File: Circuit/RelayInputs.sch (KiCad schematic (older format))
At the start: 6 parts, among them K301 Meisei-m4-24h, K302 Meisei-m4-24h, K303 Meisei-m4-24h, K304 Meisei-m4-24h, K305 Meisei-m4-24h, K306 Meisei-m4-24h

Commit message: Continued PCB work, placement started. Report and presentation also started
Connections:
- net GND: no longer K301.4 (T1common), K302.4 (T1common), K303.4 (T1common), K304.4 (T1common), K305.4 (T1common), K306.4 (T1common)
- net Input1: now also K301.4 (T1common); no longer K301.8 (T1sel2)
- net Input2: now also K302.4 (T1common); no longer K302.8 (T1sel2)
- net Input3: now also K303.4 (T1common); no longer K303.8 (T1sel2)
- net Input4: now also K304.4 (T1common); no longer K304.8 (T1sel2)
- net Input5: now also K305.4 (T1common); no longer K305.8 (T1sel2)
- net Input6: now also K306.4 (T1common); no longer K306.8 (T1sel2)
- new net +3V3: K301.8 (T1sel2), K302.8 (T1sel2), K303.8 (T1sel2), K304.8 (T1sel2), K305.8 (T1sel2), K306.8 (T1sel2)
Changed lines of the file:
@@
 EESchema Schematic File Version 2
+LIBS:ControlCircuit-rescue
 LIBS:power
 LIBS:device
@@
 L GND #PWR031
 U 1 1 58AE5323
-P 2950 2450
-F 0 "#PWR031" H 2950 2200 50  0001 C CNN
-F 1 "GND" H 2950 2300 50  0000 C CNN
-F 2 "" H 2950 2450 50  0000 C CNN
-F 3 "" H 2950 2450 50  0000 C CNN
-	1    2950 2450
-	0    1    1    0
-$EndComp
-Wire Wire Line
-	2900 2650 3100 2650
+P 2850 2550
+F 0 "#PWR031" H 2850 2300 50  0001 C CNN
+F 1 "GND" H 2850 2400 50  0000 C CNN
+F 2 "" H 2850 2550 50  0000 C CNN
+F 3 "" H 2850 2550 50  0000 C CNN
+	1    2850 2550
+	0    1    1    0
+$EndComp
 Wire Wire Line
 	3050 2250 3050 2300
 Wire Wire Line
 	3050 2300 3100 2300
-Wire Wire Line
-	2950 2450 3100 2450
-Wire Wire Line
-	3100 2550 3050 2550
-Wire Wire Line
-	3050 2550 3050 2450
-Connection ~ 3050 2450
-Text GLabel 2900 2650 0    60   Input ~ 0
+Text GLabel 2800 2300 0    60   Input ~ 0
 Input1
 NoConn ~ 4400 2450
@@
 L GND #PWR033
 U 1 1 58AE5388
-P 2950 3650
-F 0 "#PWR033" H 2950 3400 50  0001 C CNN
-F 1 "GND" H 2950 3500 50  0000 C CNN
-F 2 "" H 2950 3650 50  0000 C CNN
-F 3 "" H 2950 3650 50  0000 C CNN
-	1    2950 3650
-	0    1    1    0
-$EndComp
-Wire Wire Line
-	2900 3850 3100 3850
+P 2850 3750
+F 0 "#PWR033" H 2850 3500 50  0001 C CNN
+F 1 "GND" H 2850 3600 50  0000 C CNN
+F 2 "" H 2850 3750 50  0000 C CNN
+F 3 "" H 2850 3750 50  0000 C CNN
+	1    2850 3750
+	0    1    1    0
+$EndComp
 Wire Wire Line
 	3050 3450 3050 3500
 Wire Wire Line
 	3050 3500 3100 3500
-Wire Wire Line
-	2950 3650 3100 3650
-Wire Wire Line
-	3100 3750 3050 3750
-Wire Wire Line
-	3050 3750 3050 3650
-Connection ~ 3050 3650
-Text GLabel 2900 3850 0    60   Input ~ 0
+Text GLabel 2800 3500 0    60   Input ~ 0
 Input2
 NoConn ~ 4400 3650
@@
 L GND #PWR035
 U 1 1 58AE53E8
-P 2950 4800
-F 0 "#PWR035" H 2950 4550 50  0001 C CNN
-F 1 "GND" H 2950 4650 50  0000 C CNN
-F 2 "" H 2950 4800 50  0000 C CNN
-F 3 "" H 2950 4800 50  0000 C CNN
-	1    2950 4800
-	0    1    1    0
-$EndComp
-Wire Wire Line
-	2900 5000 3100 5000
+P 2850 4900
+F 0 "#PWR035" H 2850 4650 50  0001 C CNN
+F 1 "GND" H 2850 4750 50  0000 C CNN
+F 2 "" H 2850 4900 50  0000 C CNN
+F 3 "" H 2850 4900 50  0000 C CNN
+	1    2850 4900
+	0    1    1    0
+$EndComp
 Wire Wire Line
 	3050 4600 3050 4650
 Wire Wire Line
 	3050 4650 3100 4650
-Wire Wire Line
-	2950 4800 3100 4800
-Wire Wire Line
-	3100 4900 3050 4900
-Wire Wire Line
-	3050 4900 3050 4800
-Connection ~ 3050 4800
-Text GLabel 2900 5000 0    60   Input ~ 0
+Text GLabel 2800 4650 0    60   Input ~ 0
 Input3
 NoConn ~ 4400 4800
@@
 L GND #PWR037
 U 1 1 58AE54DC
-P 6200 2450
-F 0 "#PWR037" H 6200 2200 50  0001 C CNN
-F 1 "GND" H 6200 2300 50  0000 C CNN
-F 2 "" H 6200 2450 50  0000 C CNN
-F 3 "" H 6200 2450 50  0000 C CNN
-	1    6200 2450
-	0    1    1    0
-$EndComp
-Wire Wire Line
-	6150 2650 6350 2650
+P 6100 2550
+F 0 "#PWR037" H 6100 2300 50  0001 C CNN
+F 1 "GND" H 6100 2400 50  0000 C CNN
+F 2 "" H 6100 2550 50  0000 C CNN
+F 3 "" H 6100 2550 50  0000 C CNN
+	1    6100 2550
+	0    1    1    0
+$EndComp
 Wire Wire Line
 	6300 2250 6300 2300
 Wire Wire Line
 	6300 2300 6350 2300
-Wire Wire Line
-	6200 2450 6350 2450
-Wire Wire Line
-	6350 2550 6300 2550
-Wire Wire Line
-	6300 2550 6300 2450
-Connection ~ 6300 2450
-Text GLabel 6150 2650 0    60   Input ~ 0
+Text GLabel 6050 2300 0    60   Input ~ 0
 Input4
 NoConn ~ 7650 2450
@@
 L GND #PWR039
 U 1 1 58AE54FB
-P 6200 3650
-F 0 "#PWR039" H 6200 3400 50  0001 C CNN
-F 1 "GND" H 6200 3500 50  0000 C CNN
-F 2 "" H 6200 3650 50  0000 C CNN
-F 3 "" H 6200 3650 50  0000 C CNN
-	1    6200 3650
-	0    1    1    0
-$EndComp
-Wire Wire Line
-	6150 3850 6350 3850
+P 6100 3750
+F 0 "#PWR039" H 6100 3500 50  0001 C CNN
+F 1 "GND" H 6100 3600 50  0000 C CNN
+F 2 "" H 6100 3750 50  0000 C CNN
+F 3 "" H 6100 3750 50  0000 C CNN
+	1    6100 3750
+	0    1    1    0
+$EndComp
 Wire Wire Line
 	6300 3450 6300 3500
 Wire Wire Line
 	6300 3500 6350 3500
-Wire Wire Line
-	6200 3650 6350 3650
-Wire Wire Line
-	6350 3750 6300 3750
-Wire Wire Line
-	6300 3750 6300 3650
-Connection ~ 6300 3650
-Text GLabel 6150 3850 0    60   Input ~ 0
+Text GLabel 6050 3500 0    60   Input ~ 0
 Input5
 NoConn ~ 7650 3650
@@
 L GND #PWR041
 U 1 1 58AE551A
-P 6200 4800
-F 0 "#PWR041" H 6200 4550 50  0001 C CNN
-F 1 "GND" H 6200 4650 50  0000 C CNN
-F 2 "" H 6200 4800 50  0000 C CNN
-F 3 "" H 6200 4800 50  0000 C CNN
-	1    6200 4800
-	0    1    1    0
-$EndComp
-Wire Wire Line
-	6150 5000 6350 5000
+P 6150 4900
+F 0 "#PWR041" H 6150 4650 50  0001 C CNN
+F 1 "GND" H 6150 4750 50  0000 C CNN
+F 2 "" H 6150 4900 50  0000 C CNN
+F 3 "" H 6150 4900 50  0000 C CNN
+	1    6150 4900
+	0    1    1    0
+$EndComp
 Wire Wire Line
 	6300 4600 6300 4650
 Wire Wire Line
 	6300 4650 6350 4650
-Wire Wire Line
-	6200 4800 6350 4800
-Wire Wire Line
-	6350 4900 6300 4900
-Wire Wire Line
-	6300 4900 6300 4800
-Connection ~ 6300 4800
-Text GLabel 6150 5000 0    60   Input ~ 0
+Text GLabel 6050 4650 0    60   Input ~ 0
 Input6
 NoConn ~ 7650 4800
@@
 Text Notes 2450 5500 0    60   ~ 0
 Relay Inputs
+$Comp
+L +3.3V #PWR?
+U 1 1 58AEEFB8
+P 6150 5150
+F 0 "#PWR?" H 6150 5000 50  0001 C CNN
+F 1 "+3.3V" H 6150 5290 50  0000 C CNN
+F 2 "" H 6150 5150 50  0000 C CNN
+F 3 "" H 6150 5150 50  0000 C CNN
+	1    6150 5150
+	0    -1   -1   0
+$EndComp
+Wire Wire Line
+	6050 4650 6200 4650
+Wire Wire Line
+	6150 4900 6350 4900
+Wire Wire Line
+	6200 4650 6200 4800
+Wire Wire Line
+	6200 4800 6350 4800
+Wire Wire Line
+	6150 5150 6200 5150
+Wire Wire Line
+	6200 5150 6200 5000
+Wire Wire Line
+	6200 5000 6350 5000
+$Comp
+L +3.3V #PWR?
+U 1 1 58AEF2C8
+P 6100 4000
+F 0 "#PWR?" H 6100 3850 50  0001 C CNN
+F 1 "+3.3V" H 6100 4140 50  0000 C CNN
+F 2 "" H 6100 4000 50  0000 C CNN
+F 3 "" H 6100 4000 50  0000 C CNN
+	1    6100 4000
+	0    -1   -1   0
+$EndComp
+$Comp
+L +3.3V #PWR?
+U 1 1 58AEF2E5
+P 6100 2800
+F 0 "#PWR?" H 6100 2650 50  0001 C CNN
+F 1 "+3.3V" H 6100 2940 50  0000 C CNN
+F 2 "" H 6100 2800 50  0000 C CNN
+F 3 "" H 6100 2800 50  0000 C CNN
+	1    6100 2800
+	0    -1   -1   0
+$EndComp
+$Comp
+L +3.3V #PWR?
+U 1 1 58AEF31A
+P 2850 2800
+F 0 "#PWR?" H 2850 2650 50  0001 C CNN
+F 1 "+3.3V" H 2850 2940 50  0000 C CNN
+F 2 "" H 2850 2800 50  0000 C CNN
+F 3 "" H 2850 2800 50  0000 C CNN
+	1    2850 2800
+	0    -1   -1   0
+$EndComp
+$Comp
+L +3.3V #PWR?
+U 1 1 58AEF337
+P 2850 4000
+F 0 "#PWR?" H 2850 3850 50  0001 C CNN
+F 1 "+3.3V" H 2850 4140 50  0000 C CNN
+F 2 "" H 2850 4000 50  0000 C CNN
+F 3 "" H 2850 4000 50  0000 C CNN
+	1    2850 4000
+	0    -1   -1   0
+$EndComp
+$Comp
+L +3.3V #PWR?
+U 1 1 58AEF370
+P 2850 5150
+F 0 "#PWR?" H 2850 5000 50  0001 C CNN
+F 1 "+3.3V" H 2850 5290 50  0000 C CNN
+F 2 "" H 2850 5150 50  0000 C CNN
+F 3 "" H 2850 5150 50  0000 C CNN
+	1    2850 5150
+	0    -1   -1   0
+$EndComp
+Wire Wire Line
+	6100 3750 6350 3750
+Wire Wire Line
+	6050 3500 6150 3500
+Wire Wire Line
+	6150 3500 6150 3650
+Wire Wire Line
+	6150 3650 6350 3650
+Wire Wire Line
+	6100 4000 6150 4000
+Wire Wire Line
+	6150 4000 6150 3850
+Wire Wire Line
+	6150 3850 6350 3850
+Wire Wire Line
+	6050 2300 6150 2300
+Wire Wire Line
+	6150 2300 6150 2450
+Wire Wire Line
+	6150 2450 6350 2450
+Wire Wire Line
+	6100 2550 6350 2550
+Wire Wire Line
+	6100 2800 6150 2800
+Wire Wire Line
+	6150 2800 6150 2650
+Wire Wire Line
+	6150 2650 6350 2650
+Wire Wire Line
+	2800 2300 2900 2300
+Wire Wire Line
+	2900 2300 2900 2450
+Wire Wire Line
+	2900 2450 3100 2450
+Wire Wire Line
+	2850 2550 3100 2550
+Wire Wire Line
+	2850 2800 2900 2800
+Wire Wire Line
+	2900 2800 2900 2650
+Wire Wire Line
+	2900 2650 3100 2650
+Wire Wire Line
+	2800 3500 2900 3500
+Wire Wire Line
+	2900 3500 2900 3650
+Wire Wire Line
+	2900 3650 3100 3650
+Wire Wire Line
+	2850 3750 3100 3750
+Wire Wire Line
+	2850 4000 2900 4000
+Wire Wire Line
+	2900 4000 2900 3850
+Wire Wire Line
+	2900 3850 3100 3850
+Wire Wire Line
+	2800 4650 2900 4650
+Wire Wire Line
+	2900 4650 2900 4800
+Wire Wire Line
+	2900 4800 3100 4800
+Wire Wire Line
+	2850 4900 3100 4900
+Wire Wire Line
+	2850 5150 2900 5150
+Wire Wire Line
+	2900 5150 2900 5000
+Wire Wire Line
+	2900 5000 3100 5000
 $EndSCHEMATC

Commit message: Additional PCB work
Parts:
- added D? (x2): D, symbol D
- added K307, K308: Meisei-m4-24h, Meisei:Meisei-m4-24h, symbol Meisei-m4-24h
- added R? (x2): 2kR, symbol R
- added U301, U?: LTV-817, DIP-4, symbol LTV-817
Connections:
- net +3V3: now also K307.8 (T1sel2), K308.8 (T1sel2)
- net GND: now also K307.6 (T1sel1), K308.6 (T1sel1), U301.3, U?.3
- net GNDREF: now also K307.1 (Coil1), K308.1 (Coil1)
- net Input1 renamed I1
- net Input2 renamed I2
- net Input3 renamed I3
- net Input4 renamed I4
- net Input5 renamed I5
- net I5: now also U301.4
- net Input6 renamed I6
- net I6: now also U?.4
- net RelayInput1 renamed RI1
- net RelayInput2 renamed RI2
- net RelayInput3 renamed RI3
- net RelayInput4 renamed RI4
- net RelayInput5 renamed RI5
- net RelayInput6 renamed RI6
- new net: D?.1 (K), R?.1, U301.1
- new net: D?.1 (K), R?.1, U?.1
- new net I7: K307.4 (T1common)
- new net I8: K308.4 (T1common)
- new net RI5A: R?.2
- new net RI5K: D?.2 (A), U301.2
- new net RI6A: R?.2
- new net RI6K: D?.2 (A), U?.2
- new net RI7: K307.16 (Coil2)
- new net RI8: K308.16 (Coil2)
- no-connect marks 18 -> 24
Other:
- moved on the sheet: K301, K302, K303, K304, K305, K306

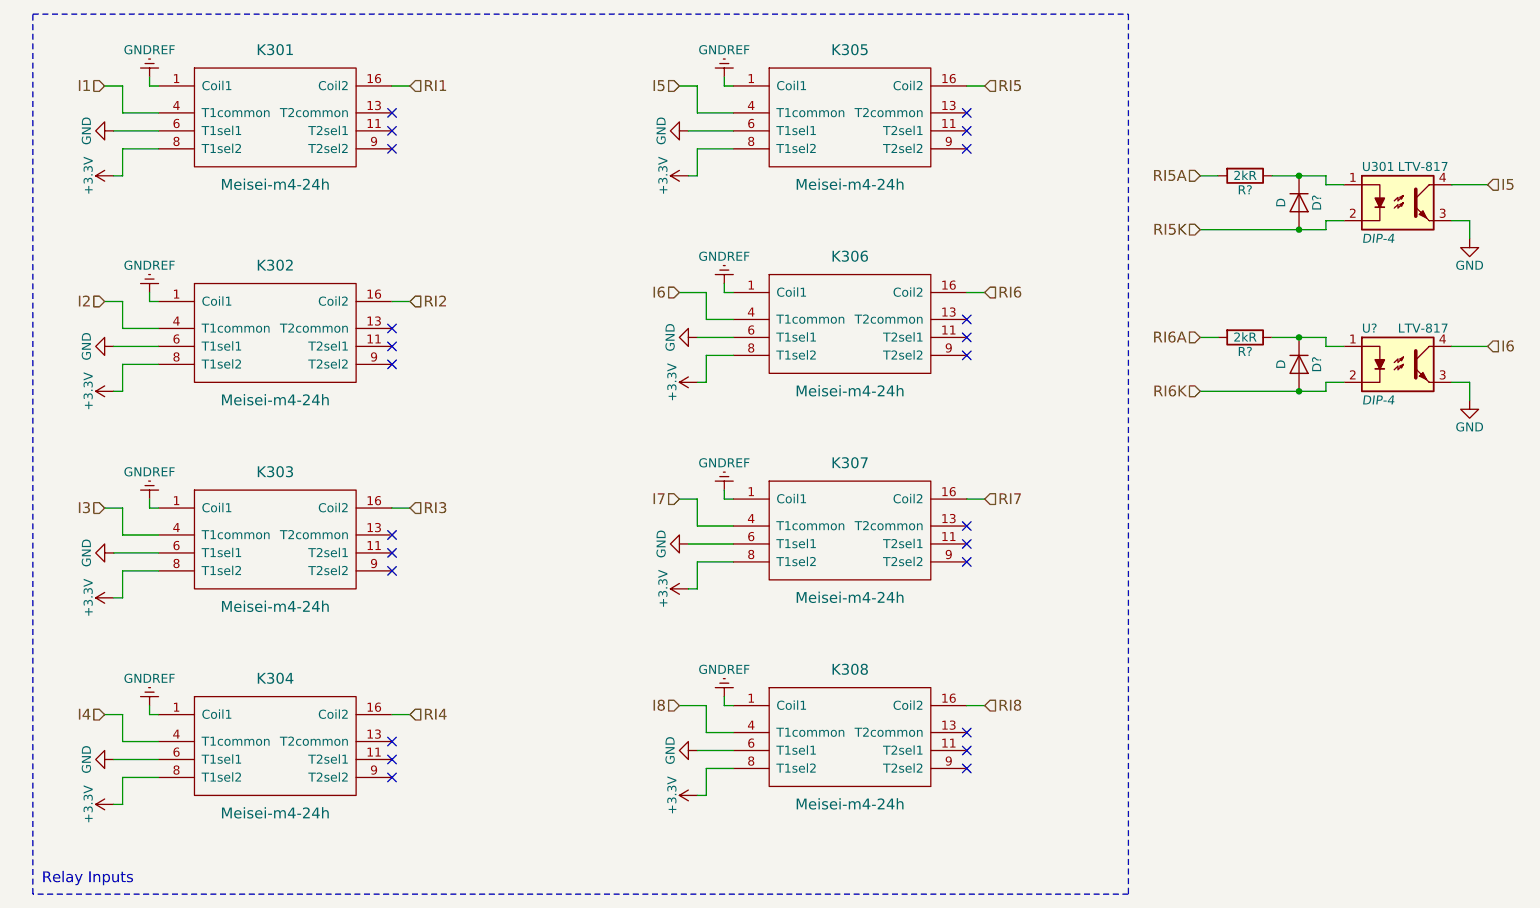
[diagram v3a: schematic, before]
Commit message: Routed PCB and made backup. Footprint for Optocouplers
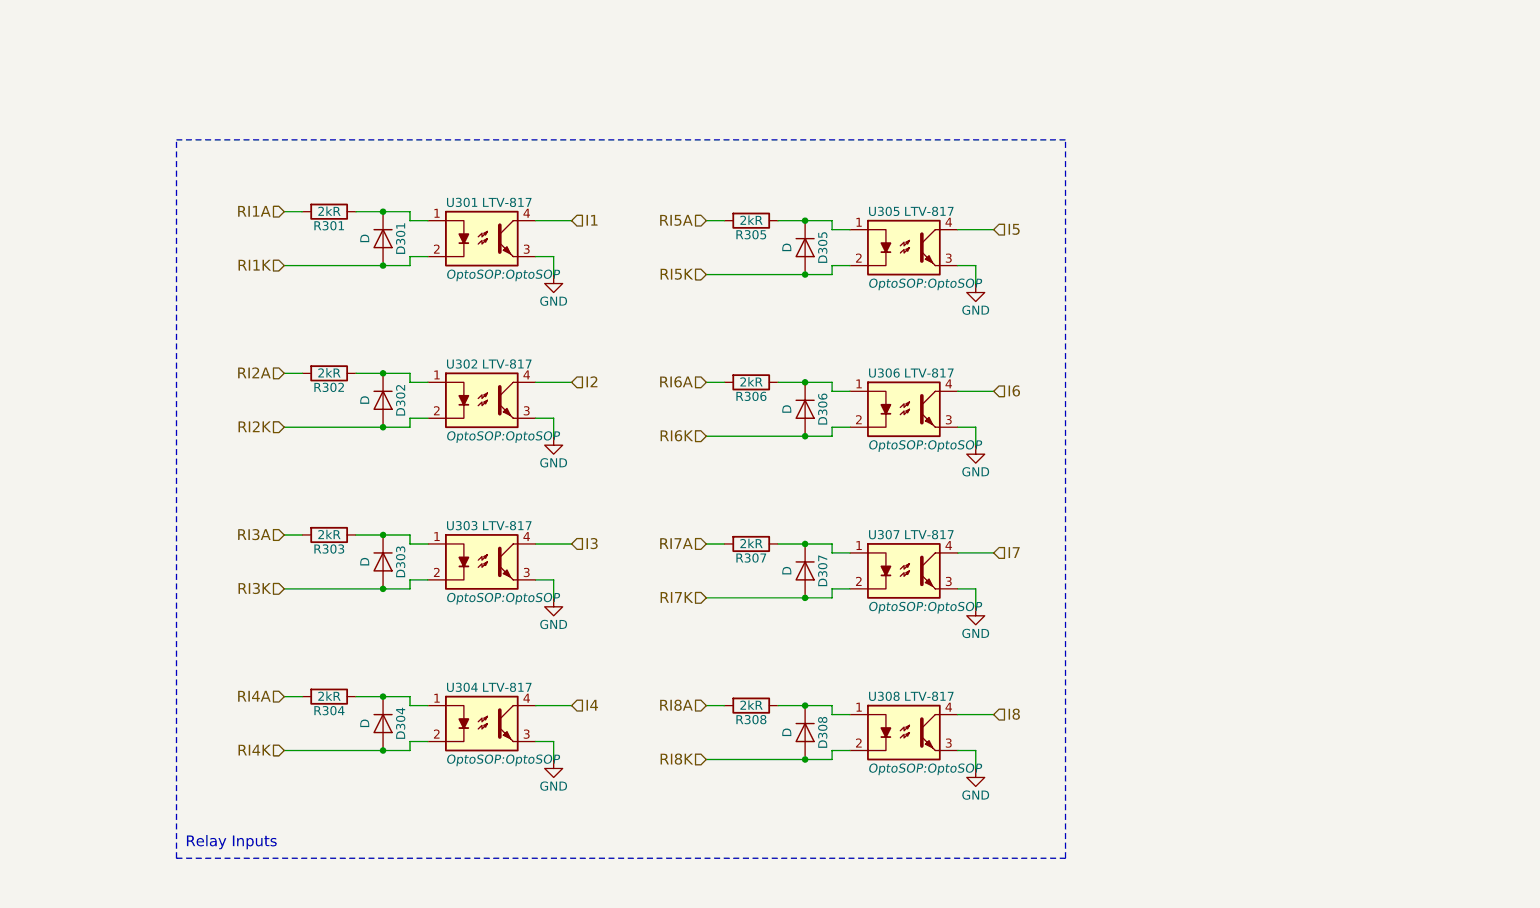
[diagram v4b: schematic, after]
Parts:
- removed K301, K302, K303, K304, K305, K306, K307, K308: Meisei-m4-24h, Meisei:Meisei-m4-24h, symbol Meisei-m4-24h
- added D301, D302, D303, D304, D307, D308: D, Diodes_SMD:D_MiniMELF_Standard, symbol D
- added R301, R302, R303, R304, R307, R308: 2kR, Resistors_SMD:R_0805, symbol R
- added U301, U302, U303, U304, U307, U308: LTV-817, OptoSOP:OptoSOP, symbol LTV-817
- D305, D306: renamed from D?; footprint (none) -> Diodes_SMD:D_MiniMELF_Standard
- R305, R306: renamed from R?; footprint (none) -> Resistors_SMD:R_0805
- U305: renamed from U301; footprint DIP-4 -> OptoSOP:OptoSOP
- U306: renamed from U?; footprint DIP-4 -> OptoSOP:OptoSOP
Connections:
- net GND: now also U301.3, U302.3, U303.3, U304.3, U307.3, U308.3
- net I1: now also U301.4
- net I2: now also U302.4
- net I3: now also U303.4
- net I4: now also U304.4
- net I7: now also U307.4
- net I8: now also U308.4
- new net: D307.1 (K), R307.1, U307.1
- new net: D308.1 (K), R308.1, U308.1
- new net: D301.1 (K), R301.1, U301.1
- new net: D302.1 (K), R302.1, U302.1
- new net: D303.1 (K), R303.1, U303.1
- new net: D304.1 (K), R304.1, U304.1
- new net RI1A: R301.2
- new net RI1K: D301.2 (A), U301.2
- new net RI2A: R302.2
- new net RI2K: D302.2 (A), U302.2
- new net RI3A: R303.2
- new net RI3K: D303.2 (A), U303.2
- new net RI4A: R304.2
- new net RI4K: D304.2 (A), U304.2
- new net RI7A: R307.2
- new net RI7K: D307.2 (A), U307.2
- new net RI8A: R308.2
- new net RI8K: D308.2 (A), U308.2
- no-connect marks 24 -> 0
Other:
- moved on the sheet: D305, D306, R305, R306, U305, U306

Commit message: PCB. Pours mostly complete. Almost done?
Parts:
- added D305, D306, D307, D308, D313, D314, D315, D316: LED, Capacitors_SMD:C_0805, symbol LED
- added R305, R306, R307, R308, R313, R314, R315, R316: 1kR, Resistors_SMD:R_0805, symbol R
- renumbered D305 to D309, D306 to D310, D307 to D311, D308 to D312, R305 to R309, R306 to R310, R307 to R311, R308 to R312
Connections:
- net I1: now also D305.1 (K)
- net I2: now also D306.1 (K)
- net I3: now also D307.1 (K)
- net I4: now also D308.1 (K)
- net I5: now also D313.1 (K)
- net I6: now also D314.1 (K)
- net I7: now also D315.1 (K)
- net I8: now also D316.1 (K)
- new net: D305.2 (A), R305.2
- new net: D307.2 (A), R307.2
- new net: D306.2 (A), R306.2
- new net: D308.2 (A), R308.2
- new net: D313.2 (A), R313.2
- new net: D314.2 (A), R314.2
- new net: D315.2 (A), R315.2
- new net: D316.2 (A), R316.2
- new net +3V3: R305.1, R306.1, R307.1, R308.1, R313.1, R314.1, R315.1, R316.1
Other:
- moved on the sheet: D302, D303, D304, D310, D311, D312, R302, R303, R304, R310, R311, R312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
